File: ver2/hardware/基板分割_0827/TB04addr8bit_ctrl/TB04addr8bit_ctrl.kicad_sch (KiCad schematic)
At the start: 12 parts, among them J101 USB_C_Receptacle_PowerOnly_6P, SW101 SW_SPDT, U101 74LS157, U102 74HC138

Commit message: ver2: 3分割で丸ごと不要なシートを削除(ctrl 3・alu 8・if 9シート)
階層ピン0のシートのみ削除。RS00/RS01は22ピンあるためGUI待ち。
差分は追加0行の純削除。

Co-Authored-By: Claude Opus 5 <noreply@anthropic.com>
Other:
- removed sheet CLK_RST
- removed sheet inPort
- removed sheet outPort
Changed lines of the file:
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@@
-	)
-	(sheet
-		(at 369.57 66.04)
-		(size 12.7 5.08)
-		(exclude_from_sim no)
-		(in_bom yes)
-		(on_board yes)
-		(dnp no)
-		(fields_autoplaced yes)
-		(stroke
-			(width 0.1524)
-			(type solid)
-		)
-		(fill
-			(color 0 0 0 0)
-		)
-		(property "Sheetname" "outPort"
-			(at 369.57 65.3284 0)
-			(show_name no)
-			(do_not_autoplace no)
-			(effects
-				(font
-					(size 1.27 1.27)
-				)
-				(justify left bottom)
-			)
-		)
-		(property "Sheetfile" "outPut.kicad_sch"
-			(at 369.57 71.7046 0)
-			(show_name no)
-			(do_not_autoplace no)
-			(effects
-				(font
-					(size 1.27 1.27)
-				)
-				(justify left top)
-			)
-		)
-		(instances
-			(project "TB04addr8bit_ctrl"
-				(path "/d176c79b-dced-4d01-bcec-7dfd676fcfc2"
-					(page "9")
-				)
-			)
-		)
 	)
 	(sheet
@@
 	)
 	(sheet
-		(at 369.57 24.13)
-		(size 12.7 3.81)
-		(exclude_from_sim no)
-		(in_bom yes)
-		(on_board yes)
-		(dnp no)
-		(fields_autoplaced yes)
-		(stroke
-			(width 0.1524)
-			(type solid)
-		)
-		(fill
-			(color 0 0 0 0)
-		)
-		(property "Sheetname" "CLK_RST"
-			(at 369.57 23.4184 0)
-			(show_name no)
-			(do_not_autoplace no)
-			(effects
-				(font
-					(size 1.27 1.27)
-				)
-				(justify left bottom)
-			)
-		)
-		(property "Sheetfile" "clk_rst.kicad_sch"
-			(at 369.57 28.5246 0)
-			(show_name no)
-			(do_not_autoplace no)
-			(effects
-				(font
-					(size 1.27 1.27)
-				)
-				(justify left top)
-			)
-		)
-		(instances
-			(project "TB04addr4bitVer3"
-				(path "/4ea1f5c4-c9b0-4258-a3d4-23d6760fc0c5"
-					(page "4")
-				)
-			)
-			(project "TB04addr8bit_ctrl"
-				(path "/d176c79b-dced-4d01-bcec-7dfd676fcfc2"
-					(page "5")
-				)
-			)
-		)
-	)
-	(sheet
 		(at 109.22 26.67)
 		(size 21.59 43.18)
@@
 				)
 			)
-		)
-	)
-	(sheet
-		(at 370.84 77.47)
-		(size 12.7 5.08)
-		(exclude_from_sim no)
-		(in_bom yes)
-		(on_board yes)
-		(dnp no)
-		(fields_autoplaced yes)
-		(stroke
-			(width 0.1524)
-			(type solid)
-		)
-		(fill
-			(color 0 0 0 0)
-		)
-		(property "Sheetname" "inPort"
-			(at 370.84 76.7584 0)
-			(show_name no)
-			(do_not_autoplace no)
-			(effects
-				(font
-					(size 1.27 1.27)
-				)
-				(justify left bottom)
-			)
-		)
-		(property "Sheetfile" "inPut.kicad_sch"
-			(at 370.84 83.1346 0)
-			(show_name no)
-			(do_not_autoplace no)
-			(effects
-				(font
-					(size 1.27 1.27)
-				)
-				(justify left top)
-			)
-		)
-		(instances
-			(project "TB04addr8bit_ctrl"
-				(path "/d176c79b-dced-4d01-bcec-7dfd676fcfc2"
-					(page "10")
-				)
-			)

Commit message: ver2: 3分割で他基板側のICを削除(ctrl 9・alu 15・if 2個)
削除前にまたぎ本数(37/20)で割り当てを検算。kicad-cliのパース通過を確認。

Co-Authored-By: Claude Opus 5 <noreply@anthropic.com>
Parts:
- removed U102: 74HC138, Package_DIP:DIP-16_W7.62mm_Socket, symbol 74xx:74HC138
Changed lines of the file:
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@@
-		)
-	)
-	(symbol
-		(lib_id "74xx:74HC138")
-		(at 266.7 147.32 0)
-		(unit 1)
-		(body_style 1)
-		(exclude_from_sim no)
-		(in_bom yes)
-		(on_board yes)
-		(in_pos_files yes)
-		(dnp no)
-		(fields_autoplaced yes)
-		(property "Reference" "U102"
-			(at 268.8433 129.54 0)
-			(show_name no)
-			(do_not_autoplace no)
-			(effects
-				(font
-					(size 1.27 1.27)
-				)
-				(justify left)
-			)
-		)
-		(property "Value" "74HC138"
-			(at 268.8433 132.08 0)
-			(show_name no)
-			(do_not_autoplace no)
-			(effects
-				(font
-					(size 1.27 1.27)
-				)
-				(justify left)
-			)
-		)
-		(property "Footprint" "Package_DIP:DIP-16_W7.62mm_Socket"
-			(at 266.7 147.32 0)
-			(hide yes)
-			(show_name no)
-			(do_not_autoplace no)
-			(effects
-				(font
-					(size 1.27 1.27)
-				)
-			)
-		)
-		(property "Datasheet" "http://www.ti.com/lit/ds/symlink/cd74hc238.pdf"
-			(at 266.7 147.32 0)
-			(hide yes)
-			(show_name no)
-			(do_not_autoplace no)
-			(effects
-				(font
-					(size 1.27 1.27)
-				)
-			)
-		)
-		(property "Description" "3-to-8 line decoder/multiplexer inverting, DIP-16/SOIC-16/SSOP-16"
-			(at 266.7 147.32 0)
-			(hide yes)
-			(show_name no)
-			(do_not_autoplace no)
-			(effects
-				(font
-					(size 1.27 1.27)
-				)
-			)
-		)
-		(pin "11"
-		)
-		(pin "1"
-		)
-		(pin "8"
-		)
-		(pin "5"
-		)
-		(pin "14"
-		)
-		(pin "10"
-		)
-		(pin "2"
-		)
-		(pin "4"
-		)
-		(pin "13"
-		)
-		(pin "3"
-		)
-		(pin "7"
-		)
-		(pin "6"
-		)
-		(pin "16"
-		)
-		(pin "12"
-		)
-		(pin "9"
-		)
-		(pin "15"
-		)
-		(instances
-			(project "TB04addr4bit"
-				(path "/4ea1f5c4-c9b0-4258-a3d4-23d6760fc0c5"
-					(reference "U15")
-					(unit 1)
-				)
-			)
-			(project "TB04addr8bit_ctrl"
-				(path "/d176c79b-dced-4d01-bcec-7dfd676fcfc2"
-					(reference "U102")
-					(unit 1)
-				)
-			)
 		)
 	)

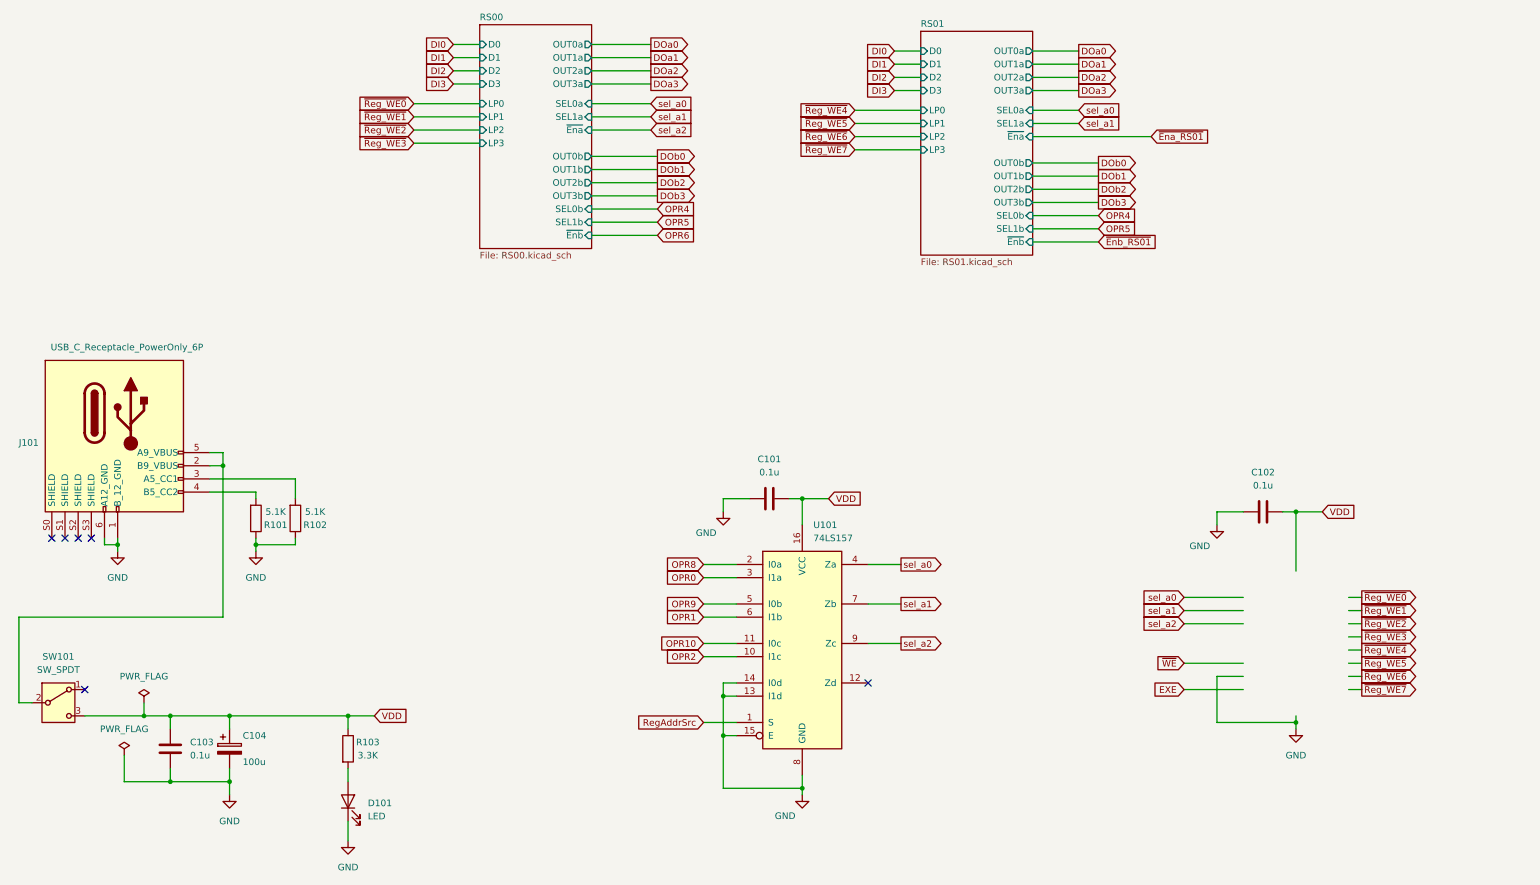
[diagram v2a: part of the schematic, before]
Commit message: ver2: 3分割でシート内の不要部品・配線を削除(検証合格)／キャリアを0827へコピー
- 制御34・演算25・IF10=IC69でマスターと一致、部品の取りこぼし0
- ピン-ネット署名の変化0件=誤って線を切った箇所なし
- またぐ信号は制御/演算35・IF/制御18で手順書の表と過不足ゼロ

Co-Authored-By: Claude Opus 5 <noreply@anthropic.com>
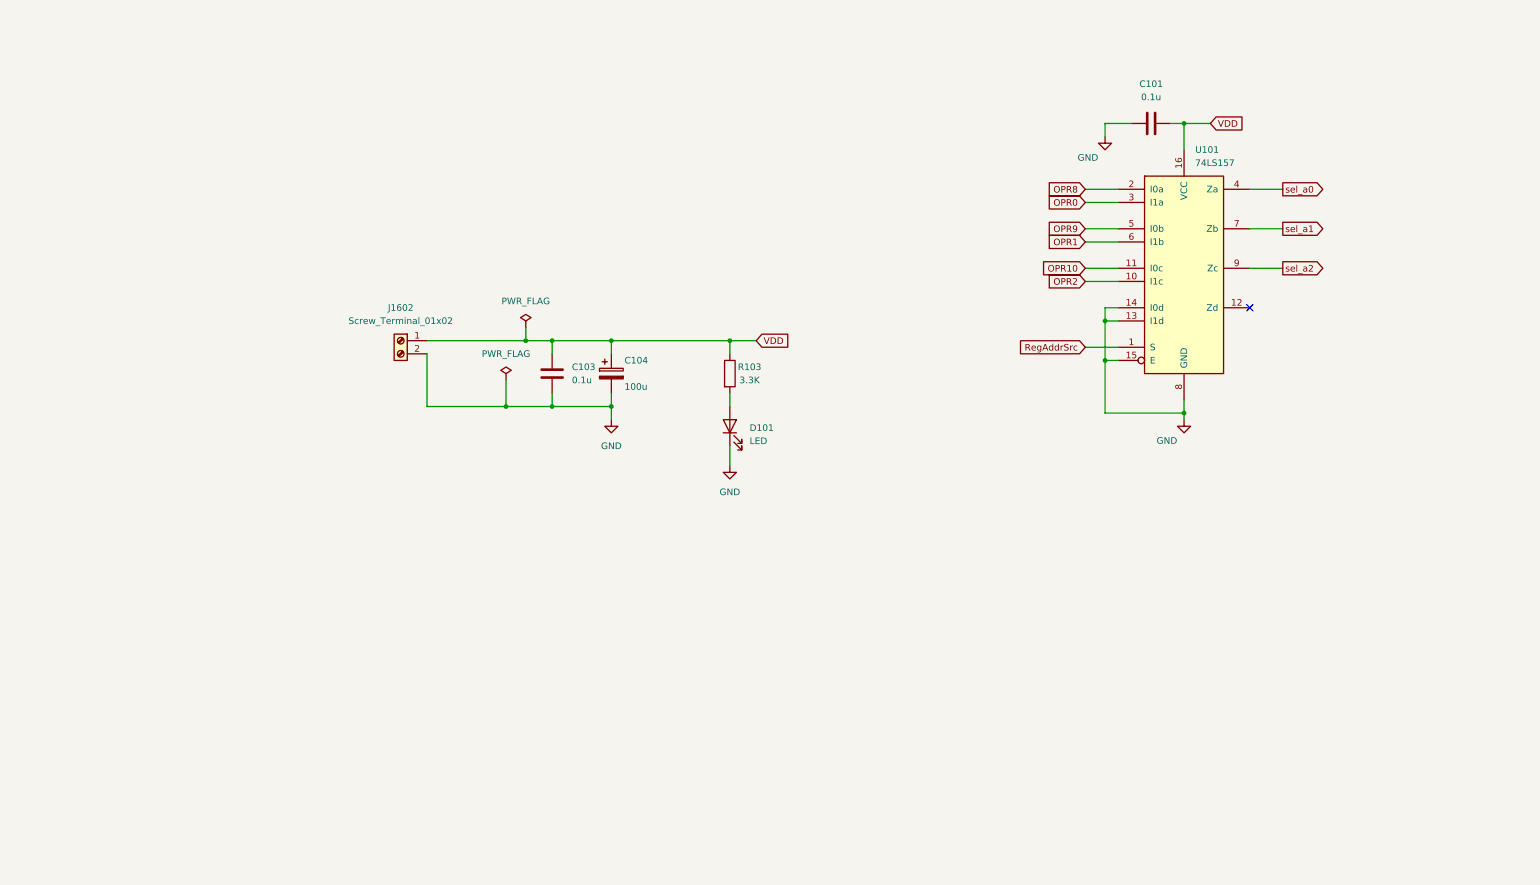
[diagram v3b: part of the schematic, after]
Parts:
- removed C102: 0.1u, Capacitor_THT:C_Disc_D4.3mm_W1.9mm_P5.00mm, symbol Device:C
- removed J101: USB_C_Receptacle_PowerOnly_6P, Library:USB_C_receptacle_onlypower_tanuki, symbol New_Library:USB_C_Receptacle_PowerOnly_6P_tanuki
- removed R101, R102: 5.1K, Resistor_THT:R_Axial_DIN0207_L6.3mm_D2.5mm_P10.16mm_Horizontal, symbol Device:R
- removed SW101: SW_SPDT, Library:sw_slide, symbol Switch:SW_SPDT
- added J1602: Screw_Terminal_01x02, symbol Connector:Screw_Terminal_01x02
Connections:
- net GND: now also J1602.2 (Pin_2)
- net VDD: now also J1602.1 (Pin_1)
- no-connect marks 6 -> 1
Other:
- removed sheet RS00
- removed sheet RS01
- moved on the sheet: C101, C103, C104, D101, R103, U101

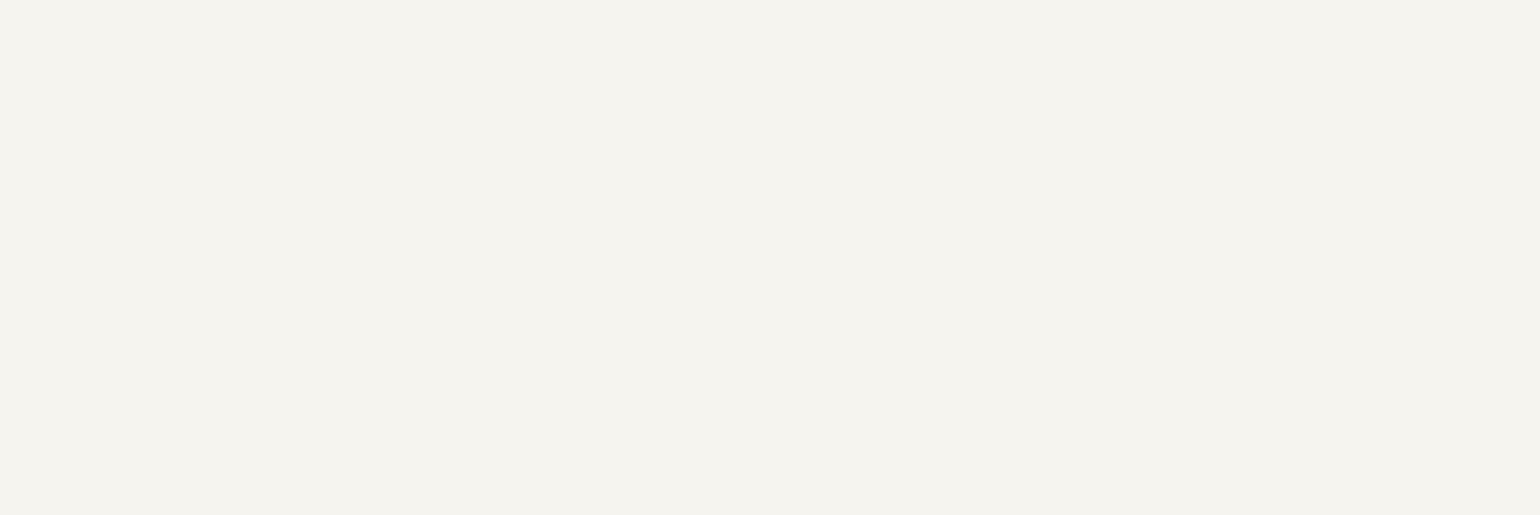
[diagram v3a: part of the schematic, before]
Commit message: ver2: 作業中の区切り(制御板のJ805-808を削除・制御板とIF板にケーブル用2x20を配置)
- 制御板: InterFaceからJ805-808を削除、J801-804(命令表示4桁)は残す
- 制御板ルートに2x20を3個、IF板ルートに2x20を1個
- 結線とai-reviewはこれから

Co-Authored-By: Claude Opus 5 <noreply@anthropic.com>
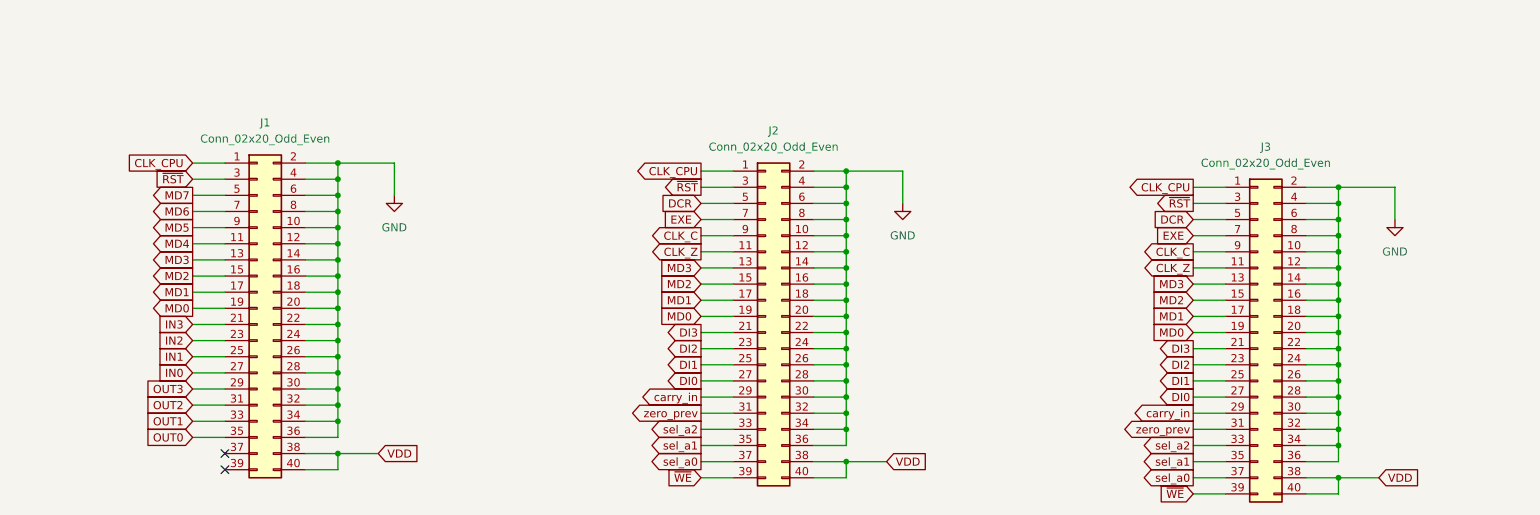
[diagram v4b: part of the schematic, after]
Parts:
- added J1, J2, J3: Conn_02x20_Odd_Even, symbol Connector_Generic:Conn_02x20_Odd_Even
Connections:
- net GND: now also J1.10 (Pin_10), J1.12 (Pin_12), J1.14 (Pin_14), J1.16 (Pin_16), J1.18 (Pin_18), J1.2 (Pin_2), J1.20 (Pin_20), J1.22 (Pin_22), J1.24 (Pin_24), J1.26 (Pin_26), J1.28 (Pin_28), J1.30 (Pin_30), J1.32 (Pin_32), J1.34 (Pin_34), J1.36 (Pin_36), J1.4 (Pin_4), J1.6 (Pin_6), J1.8 (Pin_8), J2.10 (Pin_10), J2.12 (Pin_12), J2.14 (Pin_14), J2.16 (Pin_16), J2.18 (Pin_18), J2.2 (Pin_2), J2.20 (Pin_20), J2.22 (Pin_22), J2.24 (Pin_24), J2.26 (Pin_26), J2.28 (Pin_28), J2.30 (Pin_30), J2.32 (Pin_32), J2.34 (Pin_34), J2.36 (Pin_36), J2.4 (Pin_4), J2.6 (Pin_6), J2.8 (Pin_8), J3.10 (Pin_10), J3.12 (Pin_12), J3.14 (Pin_14), J3.16 (Pin_16), J3.18 (Pin_18), J3.2 (Pin_2), J3.20 (Pin_20), J3.22 (Pin_22), J3.24 (Pin_24), J3.26 (Pin_26), J3.28 (Pin_28), J3.30 (Pin_30), J3.32 (Pin_32), J3.34 (Pin_34), J3.36 (Pin_36), J3.4 (Pin_4), J3.6 (Pin_6), J3.8 (Pin_8)
- net VDD: now also J1.38 (Pin_38), J1.40 (Pin_40), J2.38 (Pin_38), J2.40 (Pin_40), J3.38 (Pin_38), J3.40 (Pin_40)
- net sel_a0: now also J2.37 (Pin_37), J3.37 (Pin_37)
- net sel_a1: now also J2.35 (Pin_35), J3.35 (Pin_35)
- net sel_a2: now also J2.33 (Pin_33), J3.33 (Pin_33)
- new net CLK_C: J2.9 (Pin_9), J3.9 (Pin_9)
- new net CLK_CPU: J1.1 (Pin_1), J2.1 (Pin_1), J3.1 (Pin_1)
- new net CLK_Z: J2.11 (Pin_11), J3.11 (Pin_11)
- new net DCR: J2.5 (Pin_5), J3.5 (Pin_5)
- new net DI0: J2.27 (Pin_27), J3.27 (Pin_27)
- new net DI1: J2.25 (Pin_25), J3.25 (Pin_25)
- new net DI2: J2.23 (Pin_23), J3.23 (Pin_23)
- new net DI3: J2.21 (Pin_21), J3.21 (Pin_21)
- new net EXE: J2.7 (Pin_7), J3.7 (Pin_7)
- new net IN0: J1.27 (Pin_27)
- new net IN1: J1.25 (Pin_25)
- new net IN2: J1.23 (Pin_23)
- new net IN3: J1.21 (Pin_21)
- new net MD0: J1.19 (Pin_19), J2.19 (Pin_19), J3.19 (Pin_19)
- new net MD1: J1.17 (Pin_17), J2.17 (Pin_17), J3.17 (Pin_17)
- new net MD2: J1.15 (Pin_15), J2.15 (Pin_15), J3.15 (Pin_15)
- new net MD3: J1.13 (Pin_13), J2.13 (Pin_13), J3.13 (Pin_13)
- new net MD4: J1.11 (Pin_11)
- new net MD5: J1.9 (Pin_9)
- new net MD6: J1.7 (Pin_7)
- new net MD7: J1.5 (Pin_5)
- new net OUT0: J1.35 (Pin_35)
- new net OUT1: J1.33 (Pin_33)
- new net OUT2: J1.31 (Pin_31)
- new net OUT3: J1.29 (Pin_29)
- new net carry_in: J2.29 (Pin_29), J3.29 (Pin_29)
- new net zero_prev: J2.31 (Pin_31), J3.31 (Pin_31)
- new net ~{RST}: J1.3 (Pin_3), J2.3 (Pin_3), J3.3 (Pin_3)
- new net ~{WE}: J2.39 (Pin_39), J3.39 (Pin_39)
- no-connect marks 1 -> 3

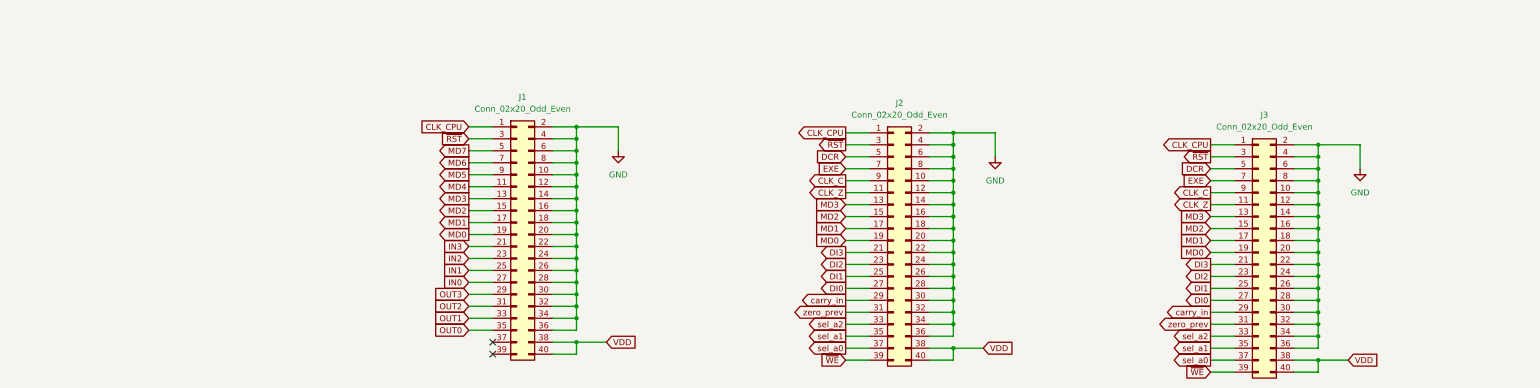
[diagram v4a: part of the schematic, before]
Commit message: ver2: 3分割にケーブル用・キャリア用コネクタを実装(検証全項目合格)
- ケーブル両端のピン割り当て100ピン全数一致、手順書の表とも不一致0
- またぐ47信号すべてコネクタに出ている(未接続0)
- isolated_pin_label 34→0、pin_not_driven 29→0

Co-Authored-By: Claude Opus 5 <noreply@anthropic.com>
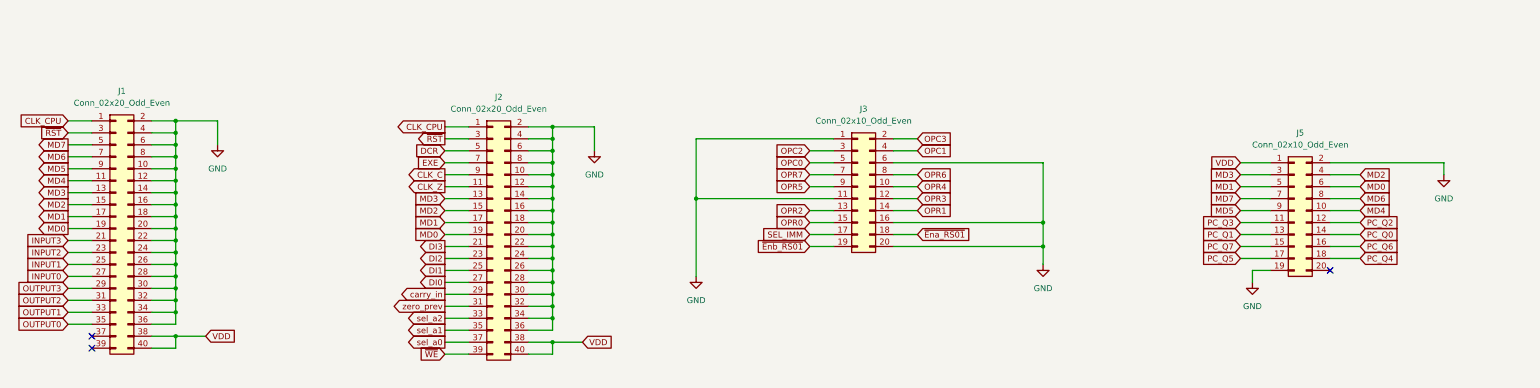
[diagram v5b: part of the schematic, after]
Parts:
- removed J3: Conn_02x20_Odd_Even, symbol Connector_Generic:Conn_02x20_Odd_Even
- added J3, J5: Conn_02x10_Odd_Even, symbol Connector_Generic:Conn_02x10_Odd_Even
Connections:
- net GND: now also J3.1 (Pin_1), J3.11 (Pin_11), J3.16 (Pin_16), J3.20 (Pin_20), J3.6 (Pin_6), J5.19 (Pin_19), J5.2 (Pin_2)
- net MD0: now also J5.6 (Pin_6)
- net MD1: now also J5.5 (Pin_5)
- net MD2: now also J5.4 (Pin_4)
- net MD3: now also J5.3 (Pin_3)
- net MD4: now also J5.10 (Pin_10)
- net MD5: now also J5.9 (Pin_9)
- net MD6: now also J5.8 (Pin_8)
- net MD7: now also J5.7 (Pin_7)
- net OPR0: now also J3.15 (Pin_15)
- net OPR1: now also J3.14 (Pin_14)
- net OPR2: now also J3.13 (Pin_13)
- net VDD: now also J5.1 (Pin_1)
- net IN0 renamed INPUT0
- net IN1 renamed INPUT1
- net IN2 renamed INPUT2
- net IN3 renamed INPUT3
- net OUT0 renamed OUTPUT0
- net OUT1 renamed OUTPUT1
- net OUT2 renamed OUTPUT2
- net OUT3 renamed OUTPUT3
- new net OPC0: J3.5 (Pin_5)
- new net OPC1: J3.4 (Pin_4)
- new net OPC2: J3.3 (Pin_3)
- new net OPC3: J3.2 (Pin_2)
- new net OPR3: J3.12 (Pin_12)
- new net OPR4: J3.10 (Pin_10)
- new net OPR5: J3.9 (Pin_9)
- new net OPR6: J3.8 (Pin_8)
- new net OPR7: J3.7 (Pin_7)
- new net PC_Q0: J5.14 (Pin_14)
- new net PC_Q1: J5.13 (Pin_13)
- new net PC_Q2: J5.12 (Pin_12)
- new net PC_Q3: J5.11 (Pin_11)
- new net PC_Q4: J5.18 (Pin_18)
- new net PC_Q5: J5.17 (Pin_17)
- new net PC_Q6: J5.16 (Pin_16)
- new net PC_Q7: J5.15 (Pin_15)
- new net SEL_IMM: J3.17 (Pin_17)
- new net ~{Ena_RS01}: J3.18 (Pin_18)
- new net ~{Enb_RS01}: J3.19 (Pin_19)
- no-connect marks 3 -> 4
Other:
- moved on the sheet: J1, J2

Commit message: ver2: 3分割のフットプリント設定完了・取付穴を追加・PCBを作り直し
- 新規コネクタ11件のフットプリントを設定(2x20/2x10ピンソケット・端子台)
- 演算板/制御板/キャリアに取付穴MountingHole_Pad×4とGNDを追加(M3・パッド付きビア)
- 3枚のPCBをコピー元マスターのレイアウトを一掃して作り直し(配置前・配線0)
- 階層から外れて残っていたRS00/RS01.kicad_sch(制御板・IF板)を削除

検証: フットプリント未設定0件、回路図とPCBの参照番号の集合差分0
(演算102/制御101/IF127/キャリア14)、回路図の電気的変更なし

Co-Authored-By: Claude Opus 5 <noreply@anthropic.com>
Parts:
- added H101, H102, H103, H104: MountingHole_Pad, MountingHole:MountingHole_3.2mm_M3_Pad_Via, symbol Mechanical:MountingHole_Pad
- J1, J2: footprint (none) -> Connector_PinSocket_2.54mm:PinSocket_2x20_P2.54mm_Vertical
- J1602: footprint (none) -> TerminalBlock:TerminalBlock_MaiXu_MX126-5.0-02P_1x02_P5.00mm
- J3, J5: footprint (none) -> Connector_PinSocket_2.54mm:PinSocket_2x10_P2.54mm_Vertical
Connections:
- net GND: now also H101.1, H102.1, H103.1, H104.1
